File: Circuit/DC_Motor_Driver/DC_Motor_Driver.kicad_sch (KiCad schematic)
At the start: 13 parts, among them Q1 S8050, Q2 S8050, Q3 S8550, Q4 S8050, Q5 IRF540N

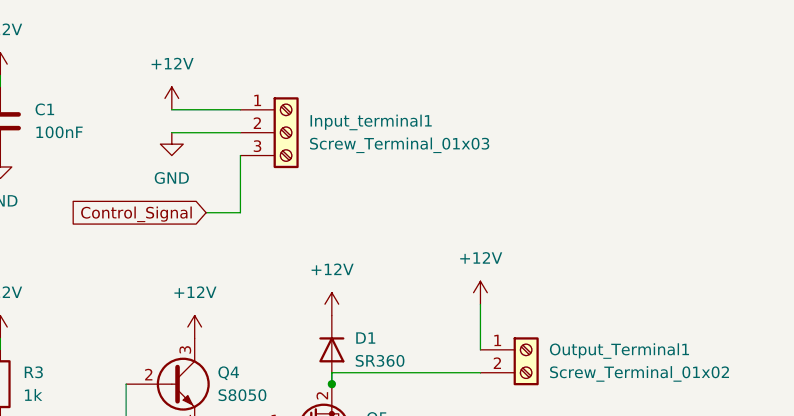
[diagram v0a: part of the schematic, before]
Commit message: Fixed DC Motor Circuit and discovered fatal design flaw in PWM demultiplexer
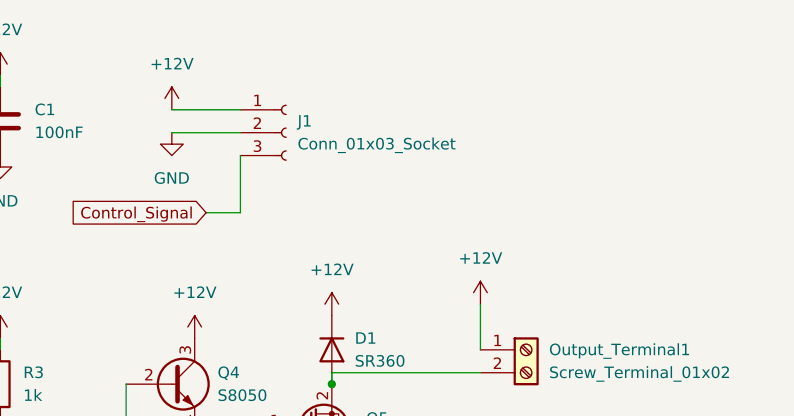
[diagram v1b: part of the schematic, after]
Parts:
- removed Input_terminal1: Screw_Terminal_01x03, TerminalBlock:TerminalBlock_bornier-3_P5.08mm, symbol Connector:Screw_Terminal_01x03
- added J1: Conn_01x03_Socket, Connector_PinSocket_2.54mm:PinSocket_1x03_P2.54mm_Horizontal, symbol Connector:Conn_01x03_Socket
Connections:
- net +12V: now also J1.1 (Pin_1)
- net Control_Signal: now also J1.3 (Pin_3)
- net GND: now also J1.2 (Pin_2)

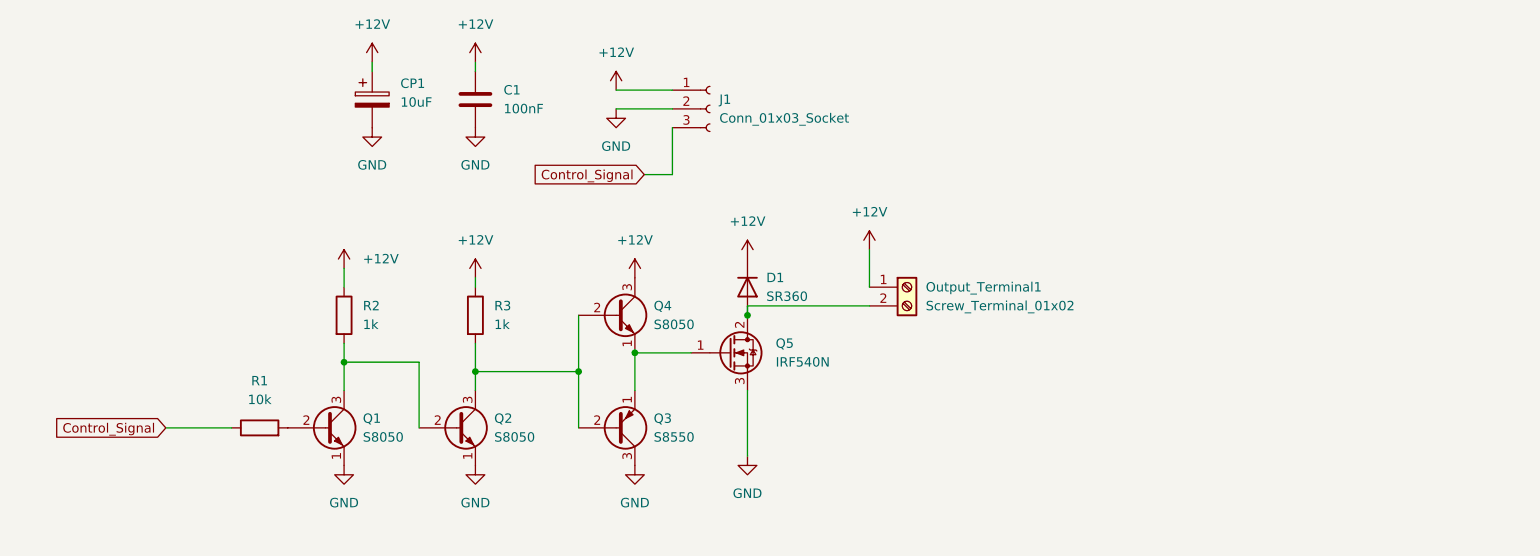
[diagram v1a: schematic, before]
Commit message: Implemented Isolators in PWM Mutliplexer
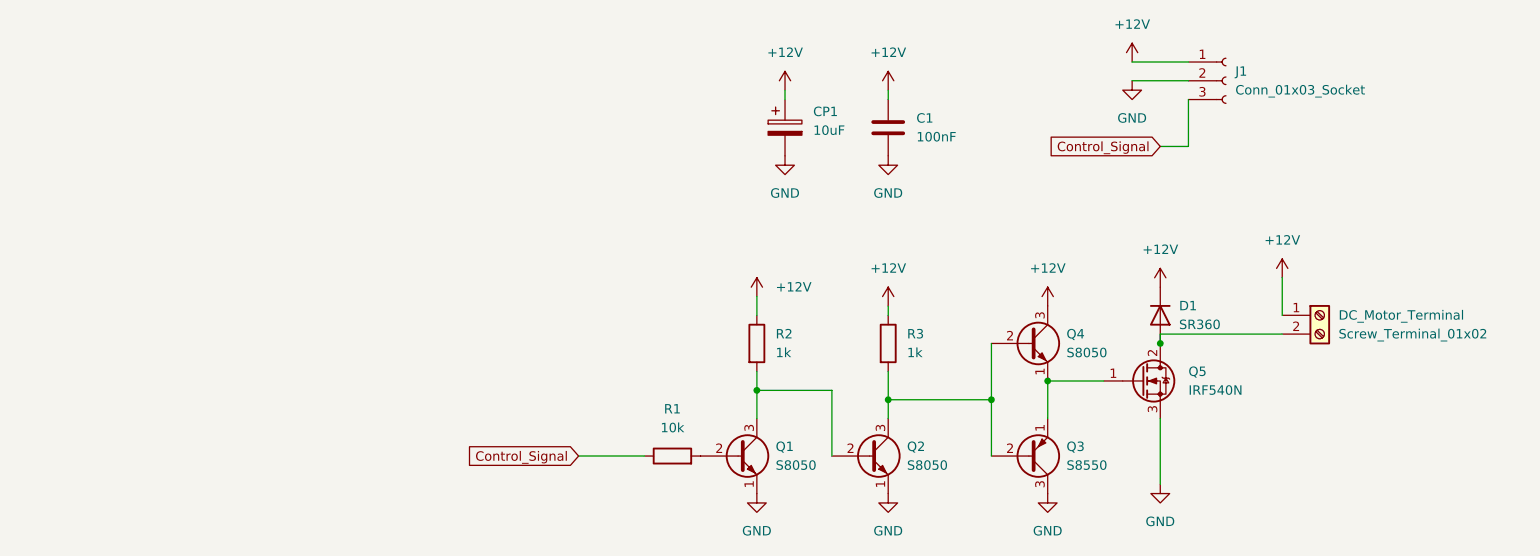
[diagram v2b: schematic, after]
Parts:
- renumbered Output_Terminal1 to DC_Motor_Terminal
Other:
- moved on the sheet: C1, CP1, D1, DC_Motor_Terminal, J1, Q1, Q2, Q3, Q4, Q5, R1, R2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

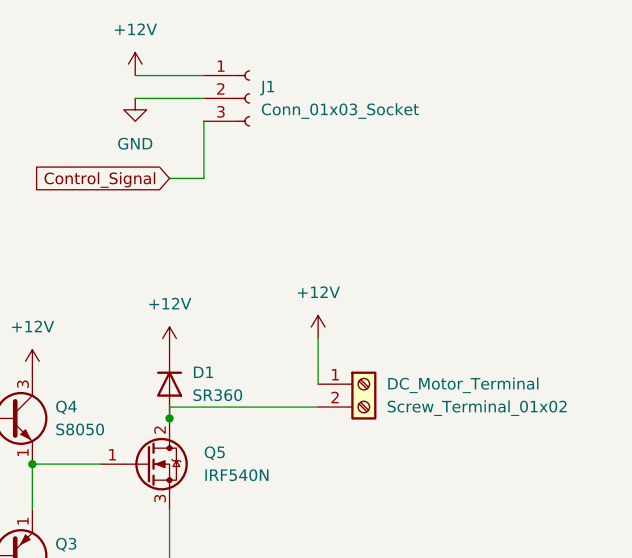
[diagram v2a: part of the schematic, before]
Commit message: DC Motor Driver Circuit fine tuning for manufacturing
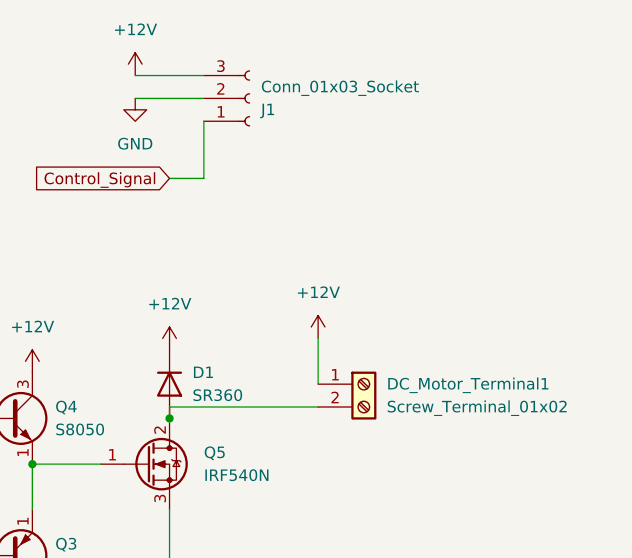
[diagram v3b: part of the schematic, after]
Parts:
- J1: footprint Connector_PinSocket_2.54mm:PinSocket_1x03_P2.54mm_Horizontal -> Connector_JST:JST_EH_S3B-EH_1x03_P2.50mm_Horizontal
- renumbered DC_Motor_Terminal to DC_Motor_Terminal1
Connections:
- net +12V: now also J1.3 (Pin_3); no longer J1.1 (Pin_1)
- net Control_Signal: now also J1.1 (Pin_1); no longer J1.3 (Pin_3)
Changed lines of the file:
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@@
     )
   )
-  (symbol (lib_id "Connector:Conn_01x03_Socket") (at 176.53 63.5 0) (unit 1)
-    (in_bom yes) (on_board yes) (dnp no) (fields_autoplaced)
-    (property "Reference" "J1" (at 177.8 62.23 0)
-      (effects (font (size 1.27 1.27)) (justify left))
-    )
-    (property "Value" "Conn_01x03_Socket" (at 177.8 64.77 0)
-      (effects (font (size 1.27 1.27)) (justify left))
-    )
-    (property "Footprint" "Connector_PinSocket_2.54mm:PinSocket_1x03_P2.54mm_Horizontal" (at 176.53 63.5 0)
+  (symbol (lib_id "Connector:Conn_01x03_Socket") (at 176.53 63.5 0) (mirror x) (unit 1)
+    (in_bom yes) (on_board yes) (dnp no)
+    (property "Reference" "J1" (at 177.8 64.77 0)
+      (effects (font (size 1.27 1.27)) (justify left))
+    )
+    (property "Value" "Conn_01x03_Socket" (at 177.8 62.23 0)
+      (effects (font (size 1.27 1.27)) (justify left))
+    )
+    (property "Footprint" "Connector_JST:JST_EH_S3B-EH_1x03_P2.50mm_Horizontal" (at 176.53 63.5 0)
       (effects (font (size 1.27 1.27)) hide)
     )
@@
   (symbol (lib_id "Connector:Screw_Terminal_01x02") (at 189.23 95.25 0) (unit 1)
     (in_bom yes) (on_board yes) (dnp no) (fields_autoplaced)
-    (property "Reference" "DC_Motor_Terminal" (at 191.77 95.2499 0)
+    (property "Reference" "DC_Motor_Terminal1" (at 191.77 95.2499 0)
       (effects (font (size 1.27 1.27)) (justify left))
     )
@@
       (project "DC_Motor_Driver"
         (path "/f5ea0da5-c191-4984-b9b5-8cae3da9b808"
-          (reference "DC_Motor_Terminal") (unit 1)
-        )
-      )
+          (reference "DC_Motor_Terminal1") (unit 1)
+        )
+      )
